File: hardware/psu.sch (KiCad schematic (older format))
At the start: 16 parts, among them U2 MIC5233-3.3, U4 TPS22860

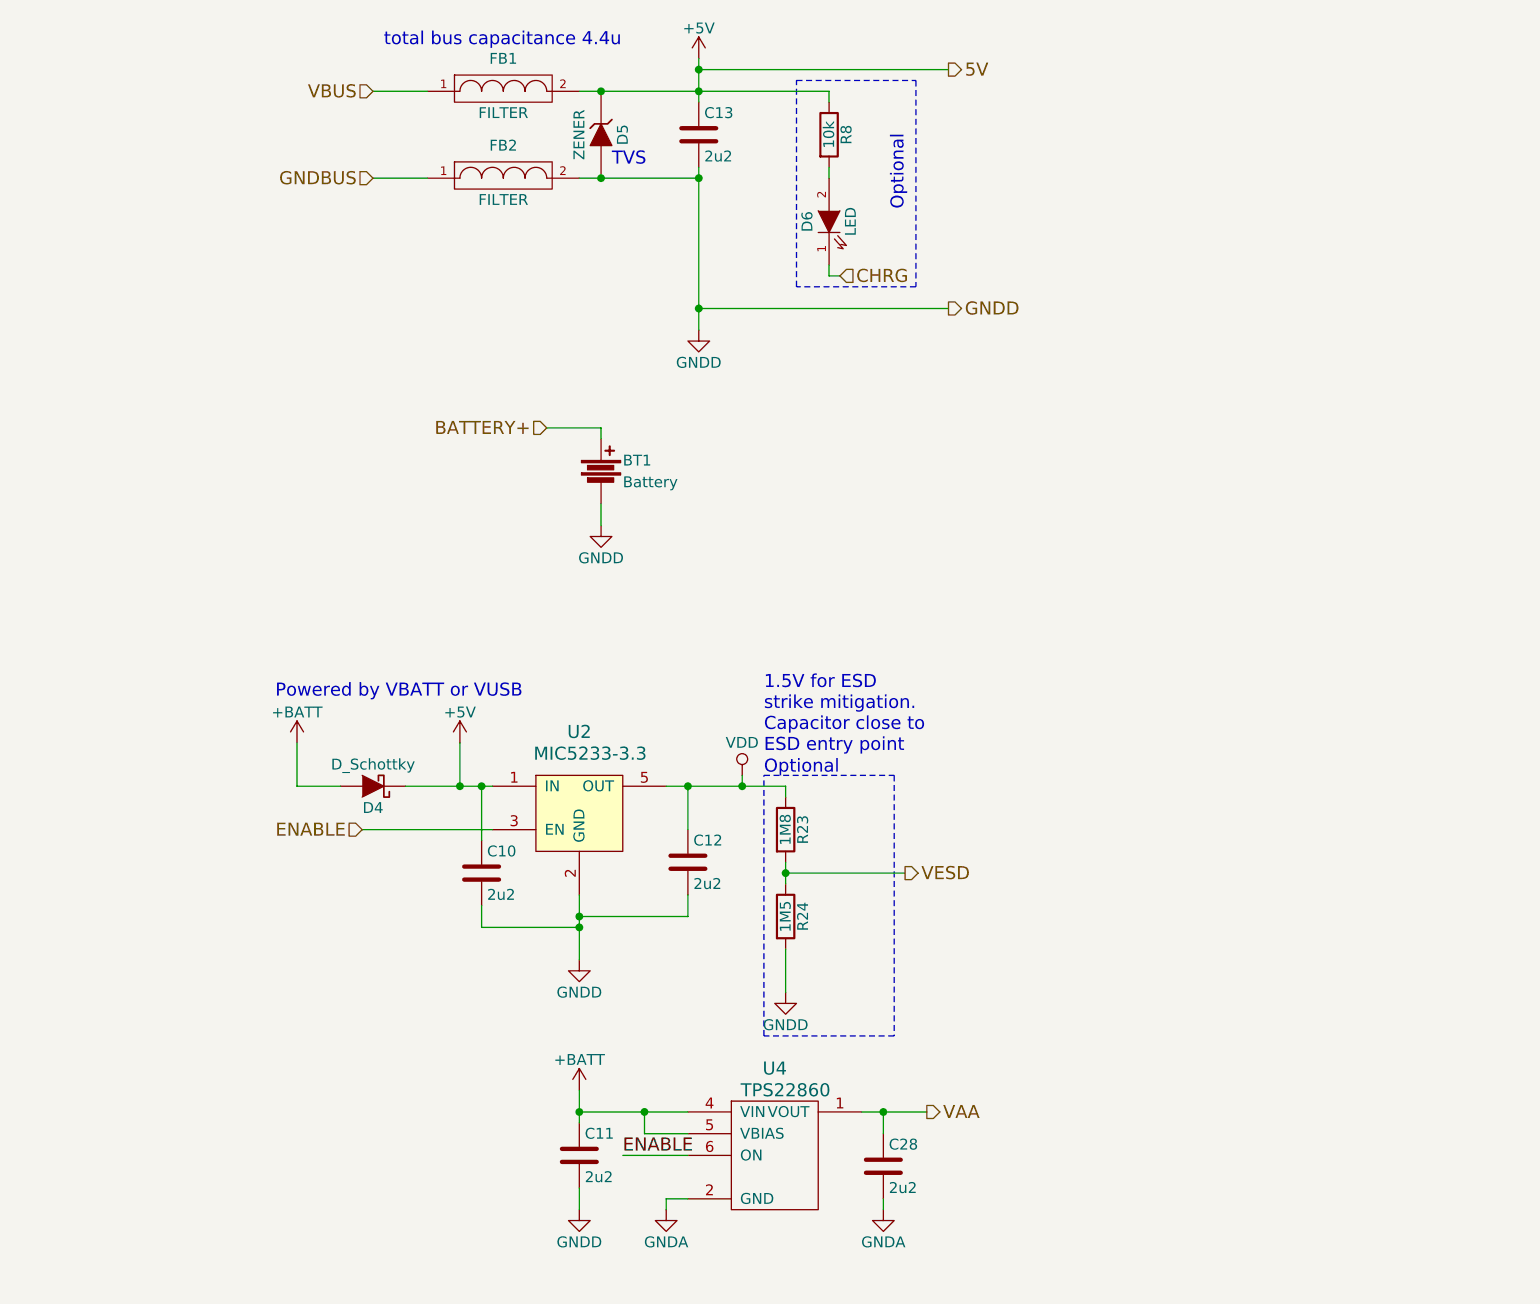
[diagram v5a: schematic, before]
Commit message: Make minimal circuitry
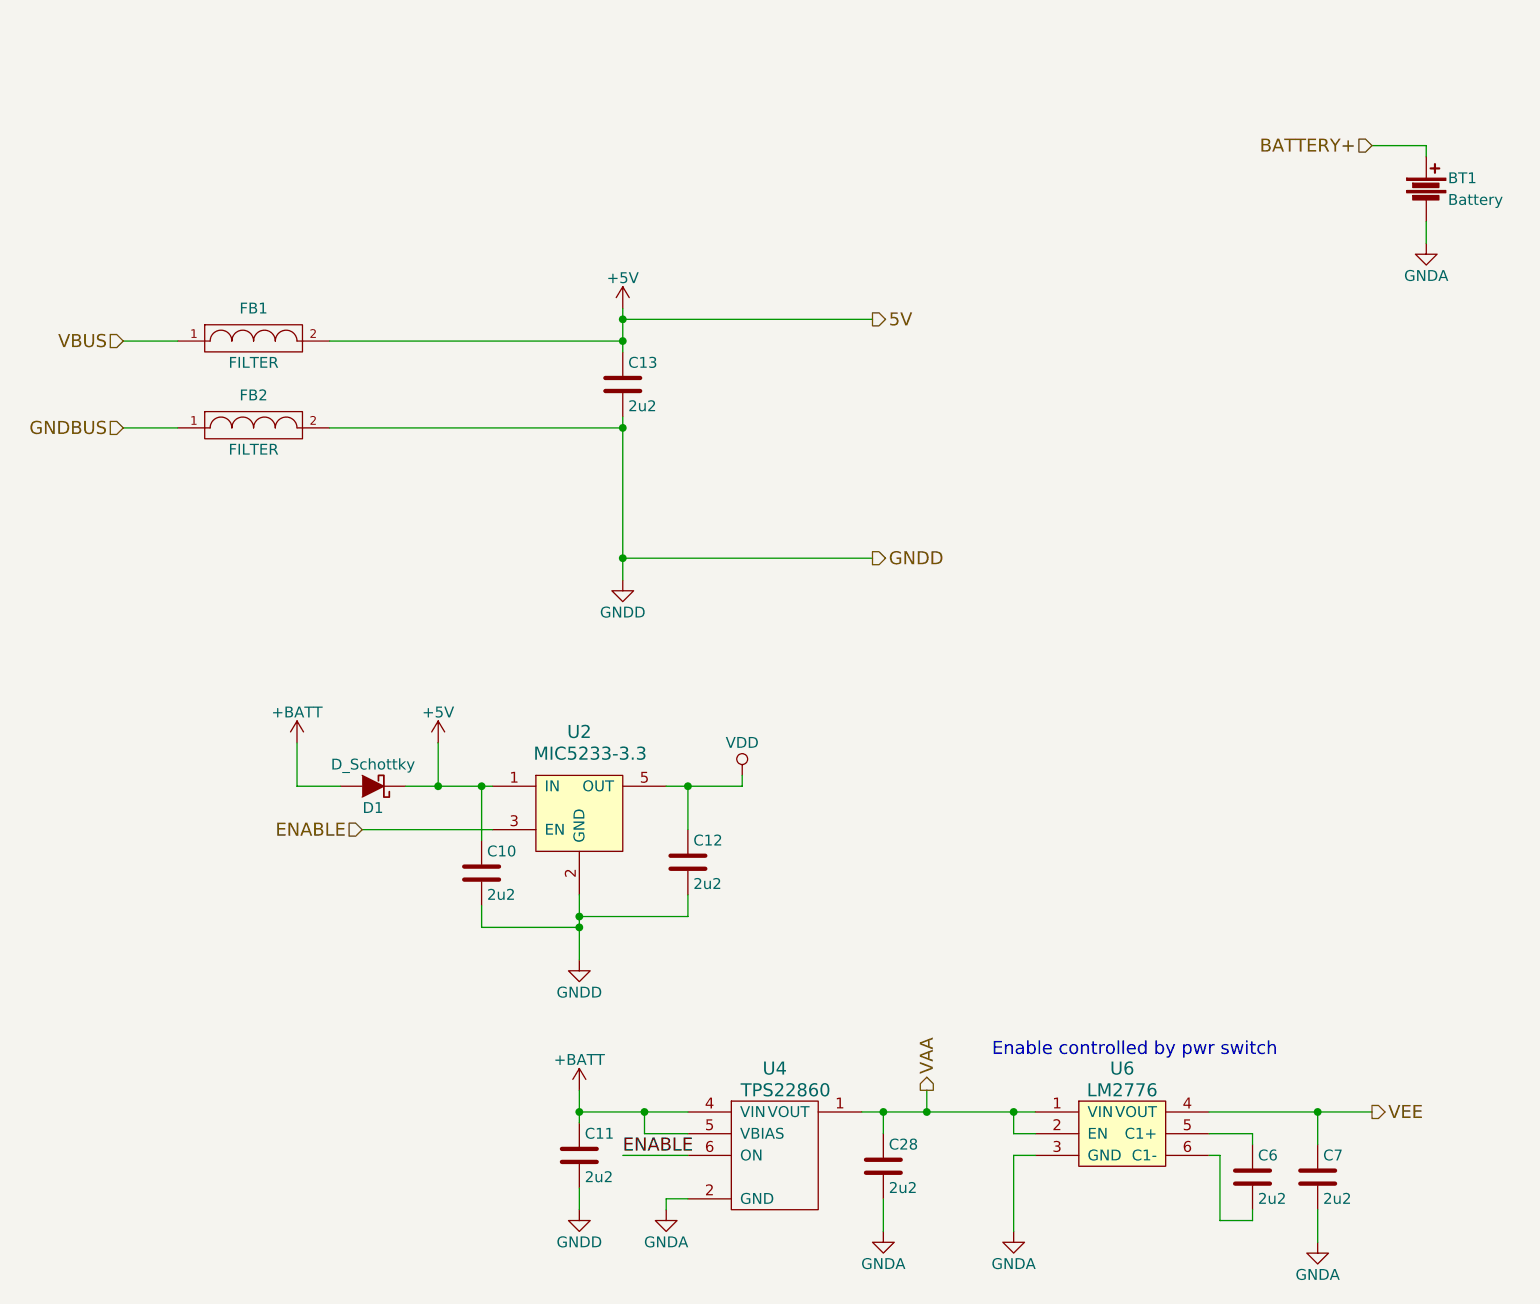
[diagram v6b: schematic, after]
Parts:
- removed D4: D_Schottky, footprints:SOD323-M, symbol D_Schottky
- removed D5: ZENER, footprints:SOD323-M, symbol ZENER
- removed D6: LED, footprints:SMD0805-LED-M, symbol LED
- removed R23: 1M8, footprints:SMD0805-RES-M, symbol R
- removed R24: 1M5, footprints:SMD0805-RES-M, symbol R
- removed R8: 10k, footprints:SMD0805-RES-M, symbol R
- added C6, C7: 2u2, footprints:SMD0402-CAP-N, symbol C
- added D1: D_Schottky, footprints:SOD323-M, symbol D_Schottky
- added U6: LM2776, footprints:SOT23-6-M, symbol LM2776
- BT1: footprint (none) -> Pin_Headers:Pin_Header_Angled_1x02
- C10, C11, C12, C13, C28: footprint footprints:SMD0805-CAP-M -> footprints:SMD0402-CAP-N
- FB1, FB2: footprint footprints:SMD0805-FERRITE-M -> footprints:SMD0402-FERRITE-N
- U4: footprint footprints:SOT23-5-M -> footprints:SOT23-6-M
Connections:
- net +5V: now also D1.1 (K)
- net +BATT: now also D1.2 (A)
- net GNDA: now also BT1.2, C7.2, U6.3 (GND)
- net GNDD: no longer BT1.2
- net VAA: now also U6.1 (VIN), U6.2 (EN)
- new net: C6.1, U6.5 (C1+)
- new net: C6.2, U6.6 (C1-)
- new net VEE: C7.1, U6.4 (VOUT)
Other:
- note added: "Enable controlled by pwr switch"
- note removed: "1.5V for ESD\nstrike mitigation.\nCapacitor close to\nESD entry point"
- note removed: "Optional"
- note removed: "Powered by VBATT or VUSB"
- note removed: "TVS"
- note removed: "total bus capacitance 4.4u"
- moved on the sheet: BT1, C13, FB1, FB2

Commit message: Finalize design
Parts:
- removed D1: D_Schottky, footprints:SOD323-M, symbol D_Schottky
- U2: footprint footprints:SOT23-6-M -> footprints:SOT23-5-M
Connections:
- net +5V: no longer C10.1, U2.1 (IN)
- net +BATT: now also C10.1, U2.1 (IN)
- net GNDA: no longer BT1.2
- net GNDD: now also BT1.2
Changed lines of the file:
@@
 F 0 "U2" H 3150 5200 60  0000 C CNN
 F 1 "MIC5233-3.3" H 3200 5100 60  0000 C CNN
-F 2 "footprints:SOT23-6-M" H 3150 4850 60  0001 C CNN
+F 2 "footprints:SOT23-5-M" H 3150 4850 60  0001 C CNN
 F 3 "" H 3150 4850 60  0000 C CNN
 	1    3150 4850
@@
 $EndComp
 $Comp
-L GNDD #PWR030
+L GNDD #PWR032
 U 1 1 573FE50E
 P 3150 5550
-F 0 "#PWR030" H 3150 5300 50  0001 C CNN
+F 0 "#PWR032" H 3150 5300 50  0001 C CNN
 F 1 "GNDD" H 3150 5400 50  0000 C CNN
 F 2 "" H 3150 5550 50  0000 C CNN
@@
 $EndComp
 $Comp
-L +BATT #PWR031
+L +BATT #PWR033
 U 1 1 573FE50F
 P 1850 4550
-F 0 "#PWR031" H 1850 4400 50  0001 C CNN
+F 0 "#PWR033" H 1850 4400 50  0001 C CNN
 F 1 "+BATT" H 1850 4690 50  0000 C CNN
 F 2 "" H 1850 4550 50  0000 C CNN
@@
 $EndComp
 $Comp
-L VDD #PWR032
+L VDD #PWR034
 U 1 1 573FE51D
 P 3900 4700
-F 0 "#PWR032" H 3900 4550 50  0001 C CNN
+F 0 "#PWR034" H 3900 4550 50  0001 C CNN
 F 1 "VDD" H 3900 4850 50  0000 C CNN
 F 2 "" H 3900 4700 50  0000 C CNN
@@
 	3150 5250 3150 5550
 Wire Wire Line
-	2350 4750 2750 4750
+	1850 4750 2750 4750
 Wire Wire Line
 	2700 4750 2700 5000
@@
 $EndComp
 $Comp
-L +BATT #PWR033
+L +BATT #PWR035
 U 1 1 573FE54B
 P 3150 6150
-F 0 "#PWR033" H 3150 6000 50  0001 C CNN
+F 0 "#PWR035" H 3150 6000 50  0001 C CNN
 F 1 "+BATT" H 3150 6290 50  0000 C CNN
 F 2 "" H 3150 6150 50  0000 C CNN
@@
 	3350 2600 4500 2600
 $Comp
-L GNDD #PWR034
+L GNDD #PWR036
 U 1 1 57401DD2
 P 3350 3800
-F 0 "#PWR034" H 3350 3550 50  0001 C CNN
+F 0 "#PWR036" H 3350 3550 50  0001 C CNN
 F 1 "GNDD" H 3350 3650 50  0000 C CNN
 F 2 "" H 3350 3800 50  0000 C CNN
@@
 $EndComp
 $Comp
-L +5V #PWR035
+L +5V #PWR037
 U 1 1 57402100
 P 3350 2550
-F 0 "#PWR035" H 3350 2400 50  0001 C CNN
+F 0 "#PWR037" H 3350 2400 50  0001 C CNN
 F 1 "+5V" H 3350 2690 50  0000 C CNN
 F 2 "" H 3350 2550 50  0000 C CNN
@@
 	7050 2150 7050 2250
 $Comp
-L GNDD #PWR036
+L GNDD #PWR038
 U 1 1 574AF4C9
 P 3150 6700
-F 0 "#PWR036" H 3150 6450 50  0001 C CNN
+F 0 "#PWR038" H 3150 6450 50  0001 C CNN
 F 1 "GNDD" H 3150 6550 50  0000 C CNN
 F 2 "" H 3150 6700 50  0000 C CNN
@@
 	4550 6650 4550 6800
 $Comp
-L GNDA #PWR037
+L GNDA #PWR039
 U 1 1 574AF85C
 P 4550 6800
-F 0 "#PWR037" H 4550 6550 50  0001 C CNN
+F 0 "#PWR039" H 4550 6550 50  0001 C CNN
 F 1 "GNDA" H 4550 6650 50  0000 C CNN
 F 2 "" H 4550 6800 50  0000 C CNN
@@
 $EndComp
 $Comp
-L GNDA #PWR038
+L GNDA #PWR040
 U 1 1 574AFAC0
 P 3550 6700
-F 0 "#PWR038" H 3550 6450 50  0001 C CNN
+F 0 "#PWR040" H 3550 6450 50  0001 C CNN
 F 1 "GNDA" H 3550 6550 50  0000 C CNN
 F 2 "" H 3550 6700 50  0000 C CNN
@@
 $EndComp
 Wire Wire Line
-	3550 4750 3900 4750
+	3550 4750 4000 4750
 Wire Wire Line
 	2000 2700 3350 2700
@@
 	6550 6700 6550 6850
 $Comp
-L GNDA #PWR039
+L GNDA #PWR041
 U 1 1 5753E3B3
 P 6550 6850
-F 0 "#PWR039" H 6550 6600 50  0001 C CNN
+F 0 "#PWR041" H 6550 6600 50  0001 C CNN
 F 1 "GNDA" H 6550 6700 50  0000 C CNN
 F 2 "" H 6550 6850 50  0000 C CNN
@@
 	5150 6450 5150 6800
 $Comp
-L GNDA #PWR040
+L GNDA #PWR042
 U 1 1 5753E59D
 P 5150 6800
-F 0 "#PWR040" H 5150 6550 50  0001 C CNN
+F 0 "#PWR042" H 5150 6550 50  0001 C CNN
 F 1 "GNDA" H 5150 6650 50  0000 C CNN
 F 2 "" H 5150 6800 50  0000 C CNN
@@
 VEE
 $Comp
-L D_Schottky D1
-U 1 1 575503A4
-P 2200 4750
-F 0 "D1" H 2200 4850 50  0000 C CNN
-F 1 "D_Schottky" H 2200 4650 50  0000 C CNN
-F 2 "footprints:SOD323-M" H 2200 4750 50  0001 C CNN
-F 3 "" H 2200 4750 50  0000 C CNN
-	1    2200 4750
-	-1   0    0    1
-$EndComp
-Wire Wire Line
-	1850 4750 2050 4750
-Wire Wire Line
-	2500 4550 2500 4750
-$Comp
-L +5V #PWR041
-U 1 1 575507C7
-P 2500 4550
-F 0 "#PWR041" H 2500 4400 50  0001 C CNN
-F 1 "+5V" H 2500 4690 50  0000 C CNN
-F 2 "" H 2500 4550 50  0000 C CNN
-F 3 "" H 2500 4550 50  0000 C CNN
-	1    2500 4550
-	1    0    0    -1
-$EndComp
-Connection ~ 2500 4750
-$Comp
-L GNDA #PWR042
-U 1 1 5757B539
+L GNDD #PWR043
+U 1 1 5753E71F
 P 7050 2250
-F 0 "#PWR042" H 7050 2000 50  0001 C CNN
-F 1 "GNDA" H 7050 2100 50  0000 C CNN
+F 0 "#PWR043" H 7050 2000 50  0001 C CNN
+F 1 "GNDD" H 7050 2100 50  0000 C CNN
 F 2 "" H 7050 2250 50  0000 C CNN
 F 3 "" H 7050 2250 50  0000 C CNN
@@
 	1    0    0    -1
 $EndComp
+Connection ~ 3900 4750
+Text HLabel 4000 4750 2    60   Output ~ 0
+VDD
 $EndSCHEMATC
